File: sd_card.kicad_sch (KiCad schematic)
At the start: 12 parts, among them J3 MicroSD_693071020811, U20 ESD204DQAR, U21 ESD204DQAR

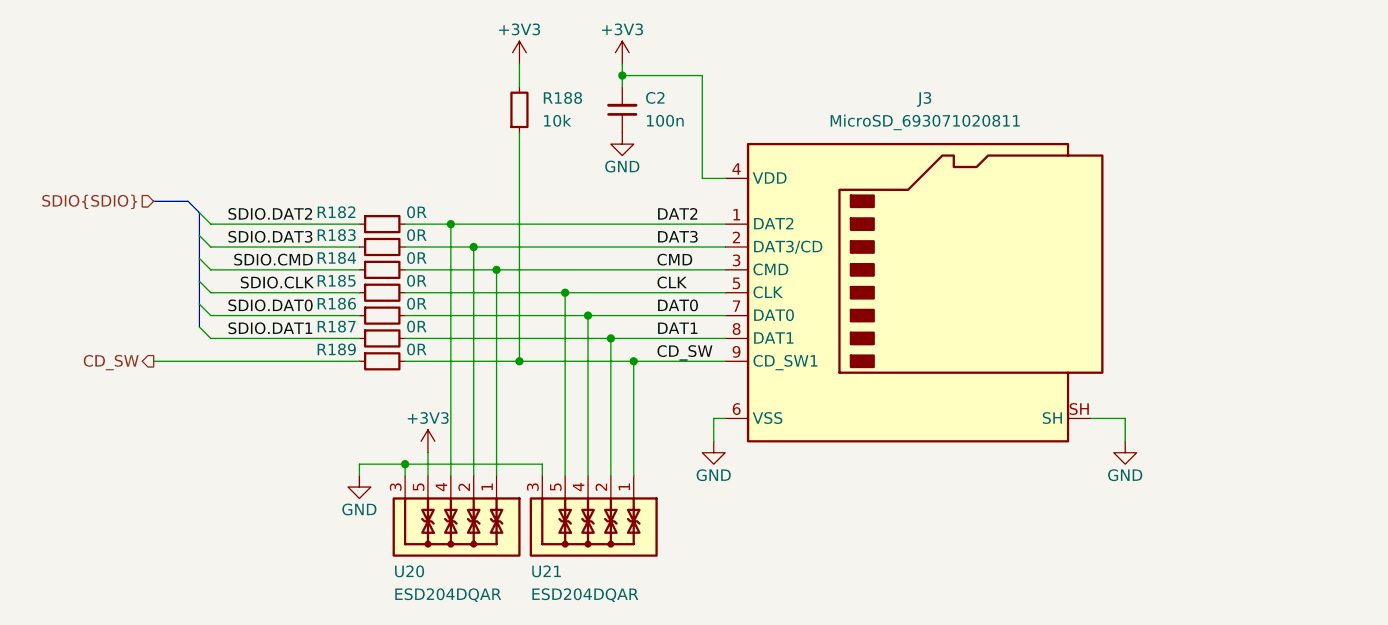
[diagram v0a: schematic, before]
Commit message: [#58137] Update backplane connector pinout
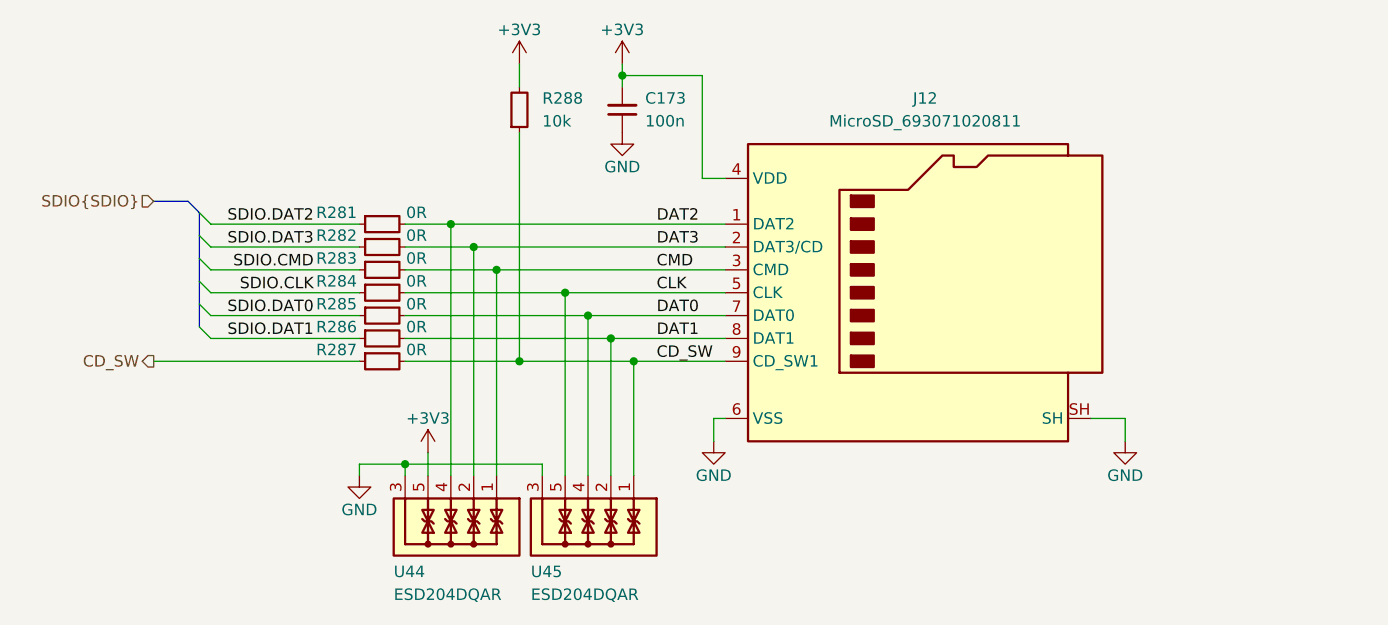
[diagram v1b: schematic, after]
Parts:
- renumbered C2 to C173, J3 to J12, R182 to R281, R183 to R282, R184 to R283, R185 to R284, R186 to R285, R187 to R286, R189 to R287, R188 to R288, U20 to U44, U21 to U45

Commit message: Reannotate schematic
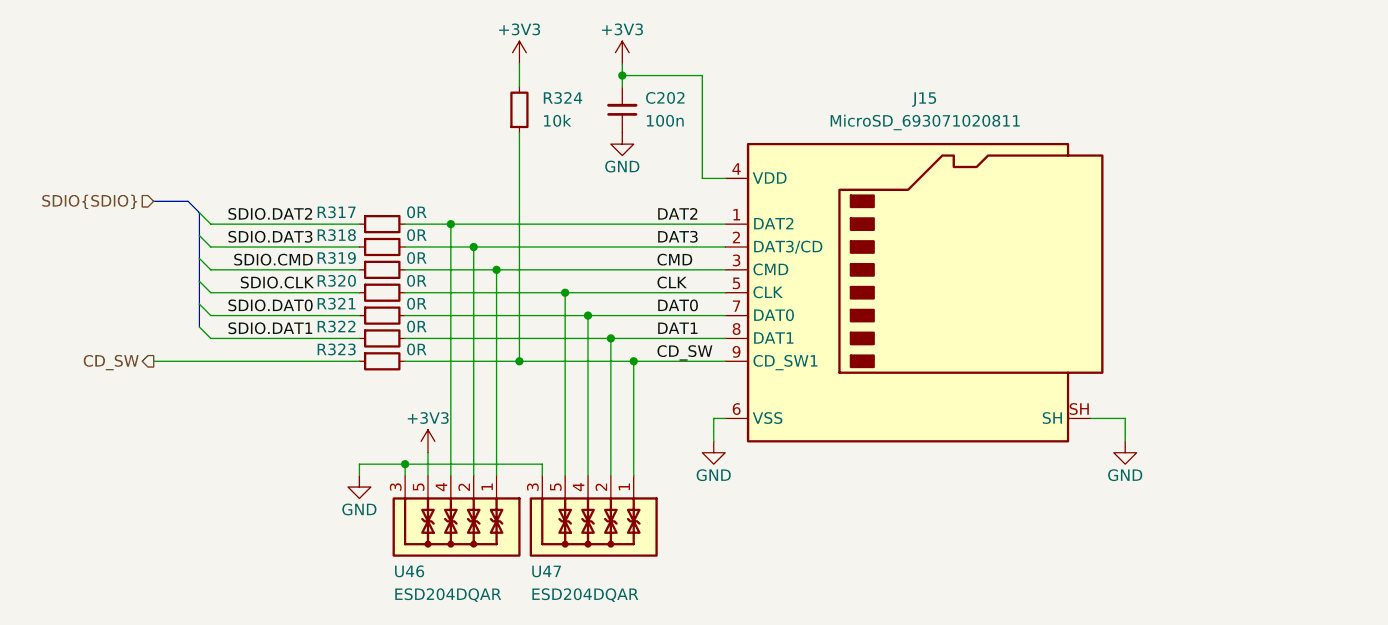
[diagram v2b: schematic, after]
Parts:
- renumbered C173 to C202, J12 to J15, R281 to R317, R282 to R318, R283 to R319, R284 to R320, R285 to R321, R286 to R322, R287 to R323, R288 to R324, U44 to U46, U45 to U47

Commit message: Optimize BOM, reannotate
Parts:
- renumbered R317 to R314, R318 to R315, R319 to R316, R320 to R317, R321 to R318, R322 to R319, R323 to R320, R324 to R321
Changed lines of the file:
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@@
   (symbol (lib_id "antmicroResistors0402:R_10k_0402") (at 215.9 132.08 90) (unit 1)
     (in_bom yes) (on_board yes) (dnp no) (fields_autoplaced)
-    (property "Reference" "R324" (at 218.44 128.27 90)
+    (property "Reference" "R321" (at 218.44 128.27 90)
       (effects (font (size 1.27 1.27) (thickness 0.15)) (justify right))
     )
@@
       (project "com-express-7-baseboard"
         (path "/1b8c34da-dad5-4b0b-8c4b-45db766c4dfa/7a16c2ca-bdcc-44db-bd2b-c6ea5f1685c3"
-          (reference "R324") (unit 1)
+          (reference "R321") (unit 1)
         )
       )
@@
   (symbol (lib_id "antmicroResistors0402:R_0R_0402") (at 198.12 152.4 0) (unit 1)
     (in_bom yes) (on_board yes) (dnp no)
-    (property "Reference" "R321" (at 195.58 151.13 0)
+    (property "Reference" "R318" (at 195.58 151.13 0)
       (effects (font (size 1.27 1.27) (thickness 0.15)))
     )
@@
       (project "com-express-7-baseboard"
         (path "/1b8c34da-dad5-4b0b-8c4b-45db766c4dfa/7a16c2ca-bdcc-44db-bd2b-c6ea5f1685c3"
-          (reference "R321") (unit 1)
+          (reference "R318") (unit 1)
         )
       )
@@
   (symbol (lib_id "antmicroResistors0402:R_0R_0402") (at 198.12 142.24 0) (unit 1)
     (in_bom yes) (on_board yes) (dnp no)
-    (property "Reference" "R317" (at 195.58 140.97 0)
+    (property "Reference" "R314" (at 195.58 140.97 0)
       (effects (font (size 1.27 1.27) (thickness 0.15)))
     )
@@
       (project "com-express-7-baseboard"
         (path "/1b8c34da-dad5-4b0b-8c4b-45db766c4dfa/7a16c2ca-bdcc-44db-bd2b-c6ea5f1685c3"
-          (reference "R317") (unit 1)
+          (reference "R314") (unit 1)
         )
       )
@@
   (symbol (lib_id "antmicroResistors0402:R_0R_0402") (at 198.12 154.94 0) (unit 1)
     (in_bom yes) (on_board yes) (dnp no)
-    (property "Reference" "R322" (at 195.58 153.67 0)
+    (property "Reference" "R319" (at 195.58 153.67 0)
       (effects (font (size 1.27 1.27) (thickness 0.15)))
     )
@@
       (project "com-express-7-baseboard"
         (path "/1b8c34da-dad5-4b0b-8c4b-45db766c4dfa/7a16c2ca-bdcc-44db-bd2b-c6ea5f1685c3"
-          (reference "R322") (unit 1)
+          (reference "R319") (unit 1)
         )
       )
@@
   (symbol (lib_id "antmicroResistors0402:R_0R_0402") (at 198.12 149.86 0) (unit 1)
     (in_bom yes) (on_board yes) (dnp no)
-    (property "Reference" "R320" (at 195.58 148.59 0)
+    (property "Reference" "R317" (at 195.58 148.59 0)
       (effects (font (size 1.27 1.27) (thickness 0.15)))
     )
@@
       (project "com-express-7-baseboard"
         (path "/1b8c34da-dad5-4b0b-8c4b-45db766c4dfa/7a16c2ca-bdcc-44db-bd2b-c6ea5f1685c3"
-          (reference "R320") (unit 1)
+          (reference "R317") (unit 1)
         )
       )
@@
   (symbol (lib_id "antmicroResistors0402:R_0R_0402") (at 198.12 144.78 0) (unit 1)
     (in_bom yes) (on_board yes) (dnp no)
-    (property "Reference" "R318" (at 195.58 143.51 0)
+    (property "Reference" "R315" (at 195.58 143.51 0)
       (effects (font (size 1.27 1.27) (thickness 0.15)))
     )
@@
       (project "com-express-7-baseboard"
         (path "/1b8c34da-dad5-4b0b-8c4b-45db766c4dfa/7a16c2ca-bdcc-44db-bd2b-c6ea5f1685c3"
-          (reference "R318") (unit 1)
+          (reference "R315") (unit 1)
         )
       )
@@
   (symbol (lib_id "antmicroResistors0402:R_0R_0402") (at 198.12 157.48 0) (unit 1)
     (in_bom yes) (on_board yes) (dnp no)
-    (property "Reference" "R323" (at 195.58 156.21 0)
+    (property "Reference" "R320" (at 195.58 156.21 0)
       (effects (font (size 1.27 1.27) (thickness 0.15)))
     )
@@
       (project "com-express-7-baseboard"
         (path "/1b8c34da-dad5-4b0b-8c4b-45db766c4dfa/7a16c2ca-bdcc-44db-bd2b-c6ea5f1685c3"
-          (reference "R323") (unit 1)
+          (reference "R320") (unit 1)
         )
       )
@@
   (symbol (lib_id "antmicroResistors0402:R_0R_0402") (at 198.12 147.32 0) (unit 1)
     (in_bom yes) (on_board yes) (dnp no)
-    (property "Reference" "R319" (at 195.58 146.05 0)
+    (property "Reference" "R316" (at 195.58 146.05 0)
       (effects (font (size 1.27 1.27) (thickness 0.15)))
     )
@@
       (project "com-express-7-baseboard"
         (path "/1b8c34da-dad5-4b0b-8c4b-45db766c4dfa/7a16c2ca-bdcc-44db-bd2b-c6ea5f1685c3"
-          (reference "R319") (unit 1)
-        )
-      )
+          (reference "R316") (unit 1)
+        )
+      )

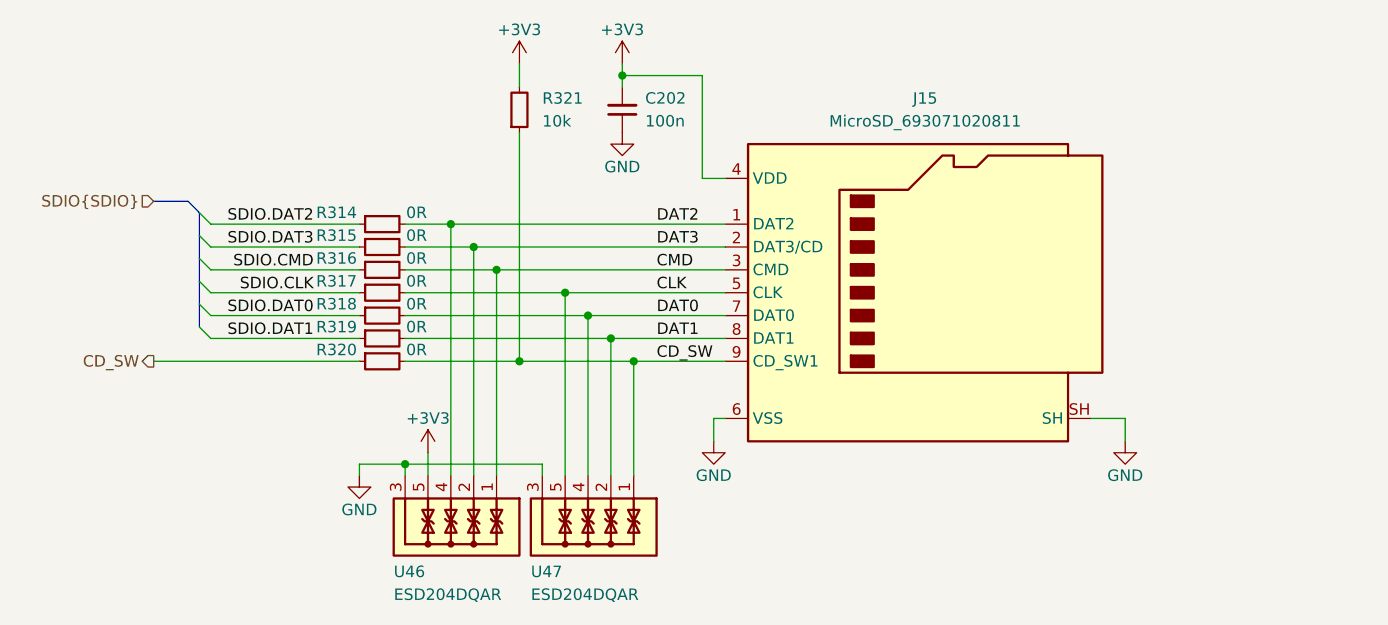
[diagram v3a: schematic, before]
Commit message: [#58904] Remove 0R on MicroSD
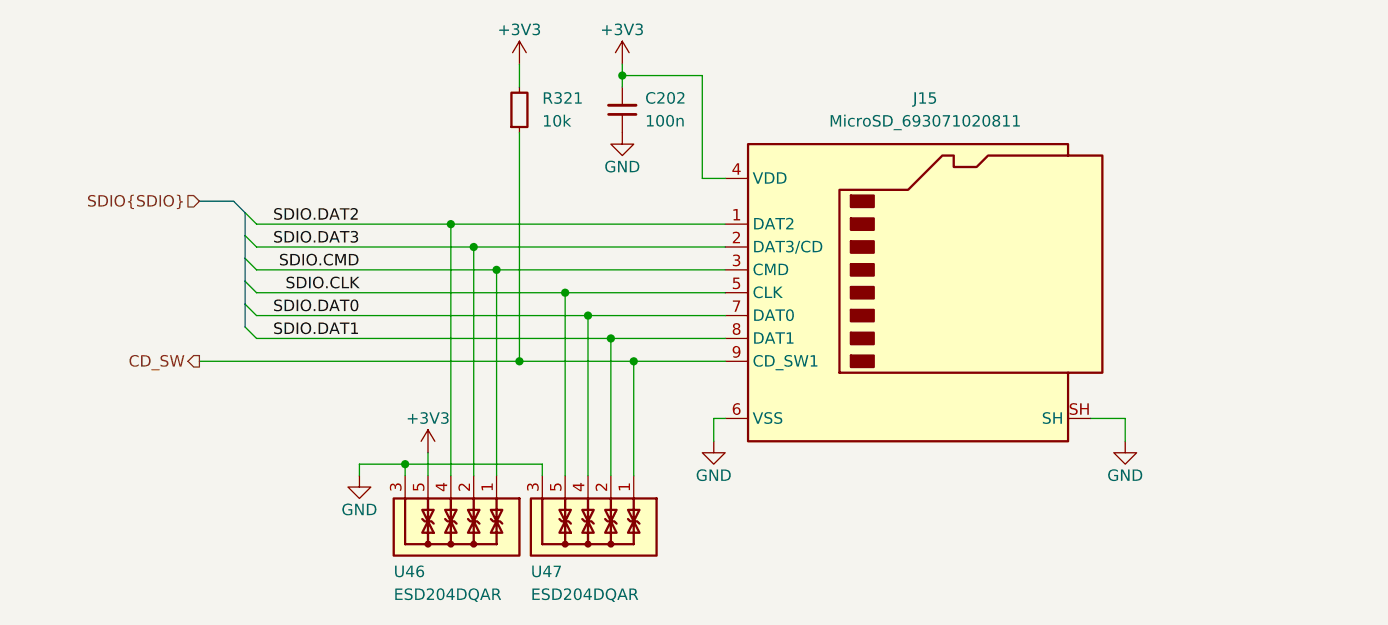
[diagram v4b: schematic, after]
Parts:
- removed R314, R315, R316, R317, R318, R319, R320: R_0R_0402, antmicro-footprints:R_0402_1005Metric, symbol antmicroResistors0402:R_0R_0402
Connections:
- net CLK is gone; now on net SDIO.CLK: J15.5 (CLK), U47.5, U47.6
- net CMD is gone; now on net SDIO.CMD: J15.3 (CMD), U46.1, U46.10
- net DAT0 is gone; now on net SDIO.DAT0: J15.7 (DAT0), U47.4, U47.7
- net DAT1 is gone; now on net SDIO.DAT1: J15.8 (DAT1), U47.2, U47.9
- net DAT2 is gone; now on net SDIO.DAT2: J15.1 (DAT2), U46.4, U46.7
- net DAT3 is gone; now on net SDIO.DAT3: J15.2 (DAT3/CD), U46.2, U46.9

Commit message: [#58904] Fix DRC
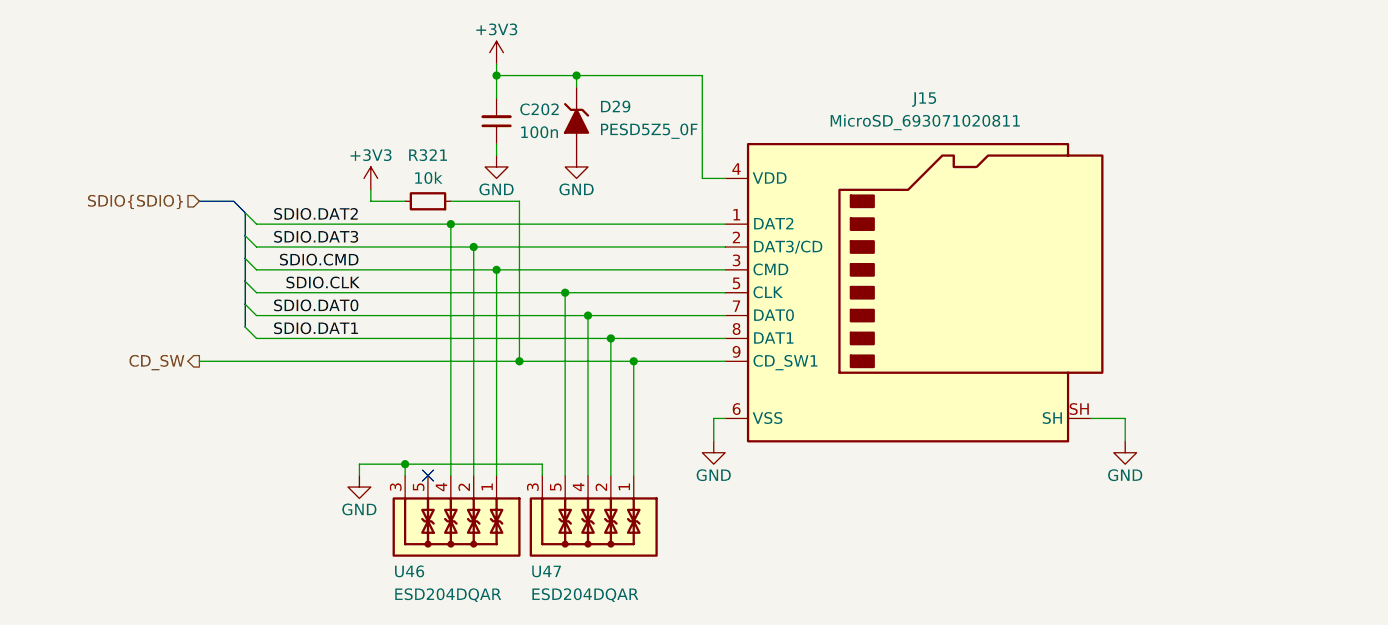
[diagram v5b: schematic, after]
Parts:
- added D29: PESD5Z5_0F, antmicro-footprints:SOD-523, symbol antmicroTVSDiodes:PESD5Z5_0F
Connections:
- net +3V3: now also D29.1; no longer U46.5, U46.6
- net GND: now also D29.2
- new net: U46.5, U46.6
- no-connect marks 0 -> 1
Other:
- moved on the sheet: C202, R321

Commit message: Update components from the library
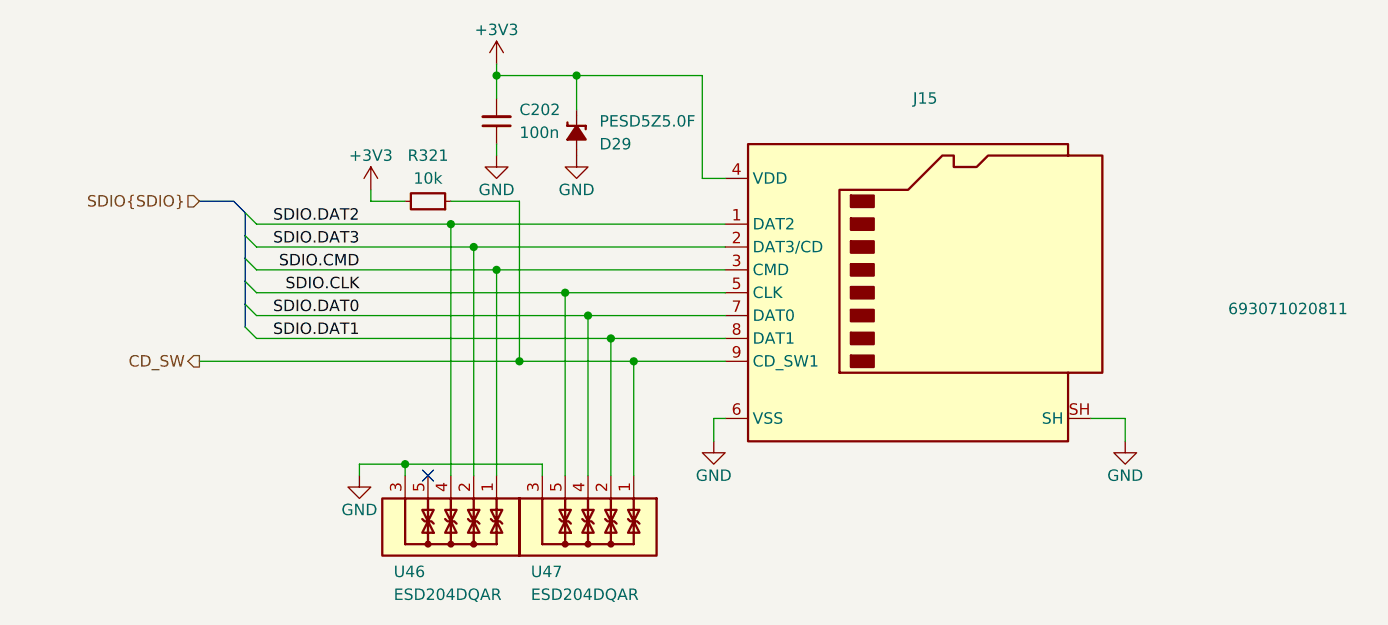
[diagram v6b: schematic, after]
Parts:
- C202, D29, R321: Public (none) -> False
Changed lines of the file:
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@@
     (stroke (width 0) (type default))
   )
-  (wire (pts (xy 222.25 125.73) (xy 222.25 127))
+  (wire (pts (xy 222.25 125.73) (xy 222.25 129.54))
     (stroke (width 0) (type default))
   )
@@
     )
     (property "Tolerance" "1%" (at 187.96 129.54 0)
+      (effects (font (size 1.27 1.27)) (justify left bottom) hide)
+    )
+    (property "Public" "False" (at 187.96 109.22 0)
       (effects (font (size 1.27 1.27)) (justify left bottom) hide)
     )
@@
     )
     (property "Value" "MicroSD_693071020811" (at 260.985 130.81 0)
-      (effects (font (size 1.27 1.27) (thickness 0.15)))
+      (effects (font (size 1.27 1.27) (thickness 0.15)) hide)
     )
     (property "Footprint" "antmicro-footprints:MicroSD_Wurth_693071020811" (at 294.64 144.78 0)
@@
     )
     (property "MPN" "693071020811" (at 294.64 152.4 0)
-      (effects (font (size 1.27 1.27) (thickness 0.15)) (justify left bottom) hide)
+      (effects (font (size 1.27 1.27) (thickness 0.15)) (justify left bottom))
     )
     (property "Author" "Antmicro" (at 294.64 154.94 0)
@@
     )
   )
-  (symbol (lib_id "antmicroTVSDiodes:PESD5Z5_0F") (at 222.25 134.62 90) (unit 1)
-    (in_bom yes) (on_board yes) (dnp no) (fields_autoplaced)
-    (property "Reference" "D29" (at 224.79 129.2224 90)
+  (symbol (lib_id "antmicroTVSDiodes:PESD5Z5_0F") (at 222.25 129.54 90) (mirror x) (unit 1)
+    (in_bom yes) (on_board yes) (dnp no)
+    (property "Reference" "D29" (at 224.79 133.35 90)
       (effects (font (size 1.27 1.27) (thickness 0.15)) (justify right))
     )
-    (property "Value" "PESD5Z5_0F" (at 224.79 131.7624 90)
+    (property "Value" "PESD5Z5_0F" (at 224.79 132.3976 90)
+      (effects (font (size 1.27 1.27) (thickness 0.15)) (justify right) hide)
+    )
+    (property "Footprint" "antmicro-footprints:SOD-523" (at 227.33 144.78 0)
+      (effects (font (size 1.27 1.27) (thickness 0.15)) (justify left bottom) hide)
+    )
+    (property "Datasheet" "https://assets.nexperia.com/documents/data-sheet/PESD5Z5_0.pdf" (at 229.87 144.78 0)
+      (effects (font (size 1.27 1.27) (thickness 0.15)) (justify left bottom) hide)
+    )
+    (property "Manufacturer" "Nexperia" (at 232.41 144.78 0)
+      (effects (font (size 1.27 1.27) (thickness 0.15)) (justify left bottom) hide)
+    )
+    (property "MPN" "PESD5Z5.0F" (at 224.79 130.81 90)
       (effects (font (size 1.27 1.27) (thickness 0.15)) (justify right))
     )
-    (property "Footprint" "antmicro-footprints:SOD-523" (at 227.33 119.38 0)
-      (effects (font (size 1.27 1.27) (thickness 0.15)) (justify left bottom) hide)
-    )
-    (property "Datasheet" "https://www.mouser.com/datasheet/2/916/PESD5Z5_0-2938691.pdf" (at 229.87 119.38 0)
-      (effects (font (size 1.27 1.27) (thickness 0.15)) (justify left bottom) hide)
-    )
-    (property "Manufacturer" "Nexperia" (at 232.41 119.38 0)
-      (effects (font (size 1.27 1.27) (thickness 0.15)) (justify left bottom) hide)
-    )
-    (property "MPN" "PESD5Z5.0F" (at 234.95 119.38 0)
-      (effects (font (size 1.27 1.27) (thickness 0.15)) (justify left bottom) hide)
-    )
-    (property "Author" "Antmicro" (at 237.49 119.38 0)
-      (effects (font (size 1.27 1.27) (thickness 0.15)) (justify left bottom) hide)
-    )
-    (property "License" "Apache-2.0" (at 240.03 119.38 0)
-      (effects (font (size 1.27 1.27) (thickness 0.15)) (justify left bottom) hide)
+    (property "Author" "Antmicro" (at 237.49 144.78 0)
+      (effects (font (size 1.27 1.27) (thickness 0.15)) (justify left bottom) hide)
+    )
+    (property "License" "Apache-2.0" (at 240.03 144.78 0)
+      (effects (font (size 1.27 1.27) (thickness 0.15)) (justify left bottom) hide)
+    )
+    (property "Public" "False" (at 240.03 149.86 0)
+      (effects (font (size 1.27 1.27)) (justify left bottom) hide)
     )
     (pin "1")
@@
     )
   )
-  (symbol (lib_name "GND_1") (lib_id "antmicropower:GND") (at 222.25 134.62 0) (mirror y) (unit 1)
+  (symbol (lib_id "antmicropower:GND") (at 222.25 134.62 0) (mirror y) (unit 1)
     (in_bom yes) (on_board yes) (dnp no)
     (property "Reference" "#PWR0264" (at 213.36 137.16 0)
@@
       (effects (font (size 1.27 1.27)) (justify left bottom) hide)
     )
+    (property "Public" "False" (at 246.38 113.03 0)
+      (effects (font (size 1.27 1.27)) (justify left bottom) hide)
+    )
